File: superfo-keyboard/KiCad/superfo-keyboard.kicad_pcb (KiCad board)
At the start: 2 copper layers, 212.7 x 84.8 mm, 12 parts

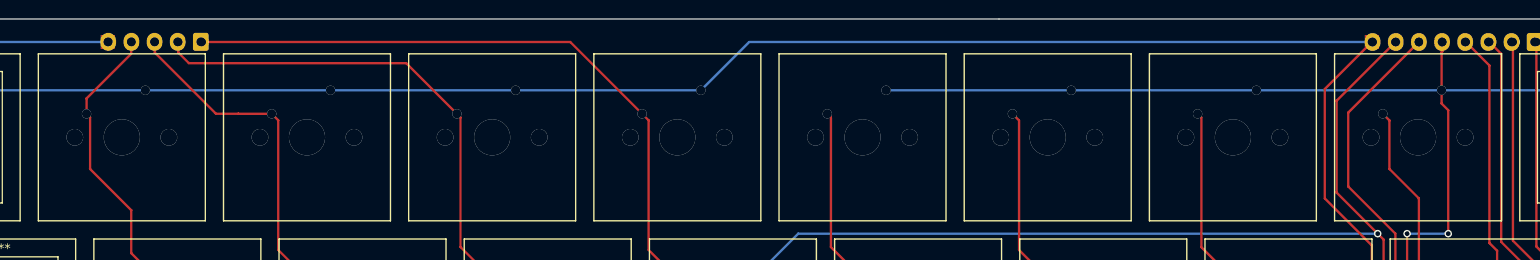
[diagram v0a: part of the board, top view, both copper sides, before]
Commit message: Add more key switches to the top row
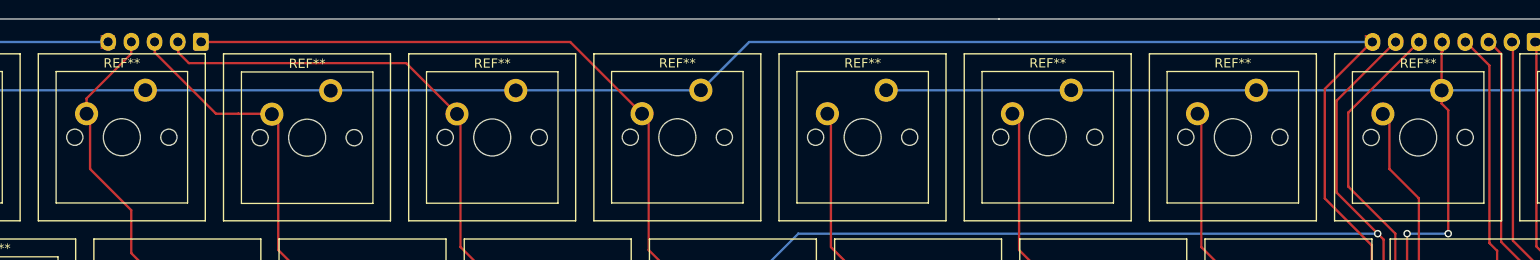
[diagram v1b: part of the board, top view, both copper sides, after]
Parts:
- added REF**: SW_Cherry_MX_PCB_1.00u, Switch_Keyboard_Cherry_MX:SW_Cherry_MX_PCB_1.00u, F.Cu at (215.7, 62.9)
- added REF**: SW_Cherry_MX_PCB_1.00u, Switch_Keyboard_Cherry_MX:SW_Cherry_MX_PCB_1.00u, F.Cu at (115.7, 62.9)
- added REF**: SW_Cherry_MX_PCB_1.00u, Switch_Keyboard_Cherry_MX:SW_Cherry_MX_PCB_1.00u, F.Cu at (155.8, 62.9)
- added REF**: SW_Cherry_MX_PCB_1.00u, Switch_Keyboard_Cherry_MX:SW_Cherry_MX_PCB_1.00u, F.Cu at (135.7, 62.9)
- added REF**: SW_Cherry_MX_PCB_1.00u, Switch_Keyboard_Cherry_MX:SW_Cherry_MX_PCB_1.00u, F.Cu at (95.8, 62.9)
- added REF**: SW_Cherry_MX_PCB_1.00u, Switch_Keyboard_Cherry_MX:SW_Cherry_MX_PCB_1.00u, F.Cu at (75.7, 62.9)
- added REF**: SW_Cherry_MX_PCB_1.00u, Switch_Keyboard_Cherry_MX:SW_Cherry_MX_PCB_1.00u, F.Cu at (175.7, 62.9)
- added REF**: SW_Cherry_MX_PCB_1.00u, Switch_Keyboard_Cherry_MX:SW_Cherry_MX_PCB_1.00u, F.Cu at (195.7, 62.9)
